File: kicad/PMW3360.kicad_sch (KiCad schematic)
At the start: 8 parts, among them J1 Conn_01x06, U1 PMW3360, U2 TCR2EF19

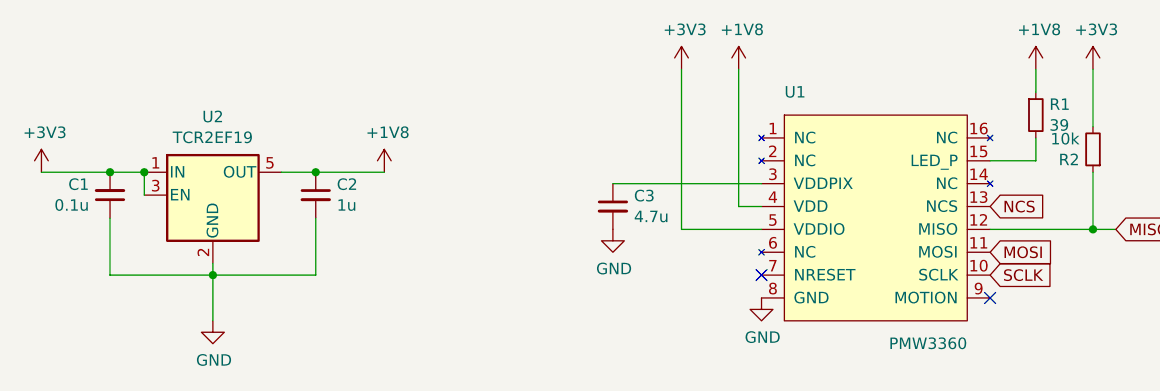
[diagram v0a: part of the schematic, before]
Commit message: Switched to JST_GH 1.25mm side-entry plug. Updated part info for the 1.8v regulator to the one that's actually available through JLCPCB.
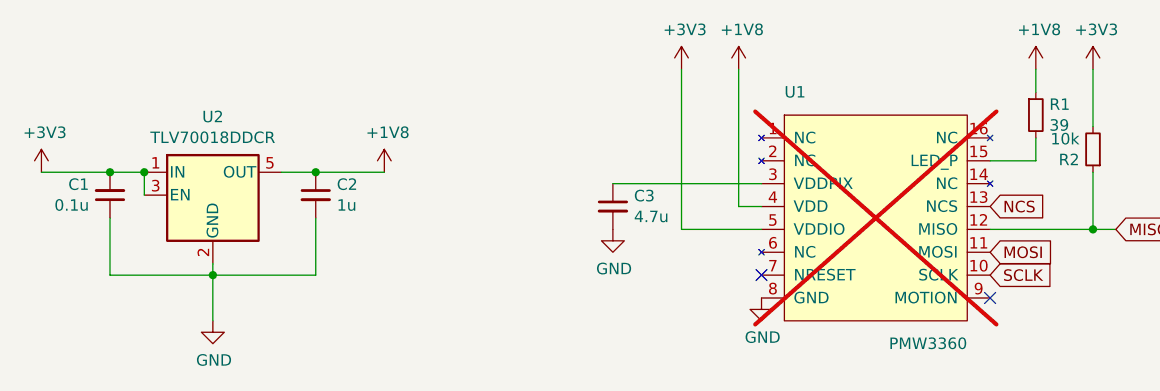
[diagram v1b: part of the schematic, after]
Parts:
- J1: footprint Connector_JST:JST_SH_BM06B-SRSS-TB_1x06-1MP_P1.00mm_Vertical -> Connector_JST:JST_GH_SM06B-GHS-TB_1x06-1MP_P1.25mm_Horizontal; LCSC (none) -> C133065
- U1: now not fitted
- U2: value TCR2EF19 -> TLV70018DDCR; symbol Regulator_Linear:TLV70218_SOT23-5 -> Regulator_Linear:TLV70018_SOT23-5; LCSC C146366 -> C79924
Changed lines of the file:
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@@
 		(in_bom yes)
 		(on_board yes)
-		(dnp no)
+		(dnp yes)
 		(property "Reference" "U1"
 			(at 133.35 86.36 0)
@@
 	)
 	(symbol
-		(lib_id "Regulator_Linear:TLV70218_SOT23-5")
+		(lib_id "Regulator_Linear:TLV70018_SOT23-5")
 		(at 69.85 97.79 0)
 		(unit 1)
@@
 			)
 		)
-		(property "Value" "TCR2EF19"
+		(property "Value" "TLV70018DDCR"
 			(at 69.85 91.4146 0)
 			(effects
@@
 			)
 		)
-		(property "Datasheet" ""
+		(property "Datasheet" "http://www.ti.com/lit/ds/symlink/tlv700.pdf"
 			(at 69.85 96.52 0)
 			(effects
@@
 			)
 		)
-		(property "Description" ""
+		(property "Description" "200mA Low Dropout Voltage Regulator, Fixed Output 1.8V, SOT-23-5"
 			(at 69.85 97.79 0)
 			(effects
@@
 			)
 		)
-		(property "LCSC" "C146366"
+		(property "LCSC" "C79924"
 			(at 69.85 97.79 0)
 			(effects
@@
 			)
 		)
-		(property "Footprint" "Connector_JST:JST_SH_BM06B-SRSS-TB_1x06-1MP_P1.00mm_Vertical"
+		(property "Footprint" "Connector_JST:JST_GH_SM06B-GHS-TB_1x06-1MP_P1.25mm_Horizontal"
 			(at 215.9 99.06 0)
 			(effects
@@
 			(at 215.9 99.06 0)
 			(effects
+				(font
+					(size 1.27 1.27)
+				)
+				(hide yes)
+			)
+		)
+		(property "LCSC" "C133065"
+			(at 215.9 99.06 0)
+			(effects

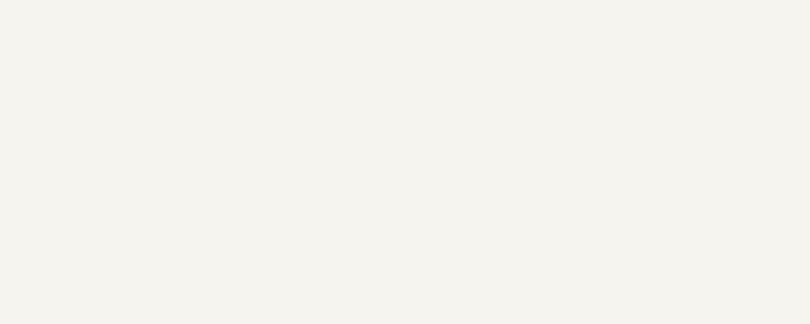
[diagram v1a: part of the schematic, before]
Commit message: Change back to JST SH 1.0mm pitch connector Use top-side 3.3v fill zone for simpler routing add .gitignore file
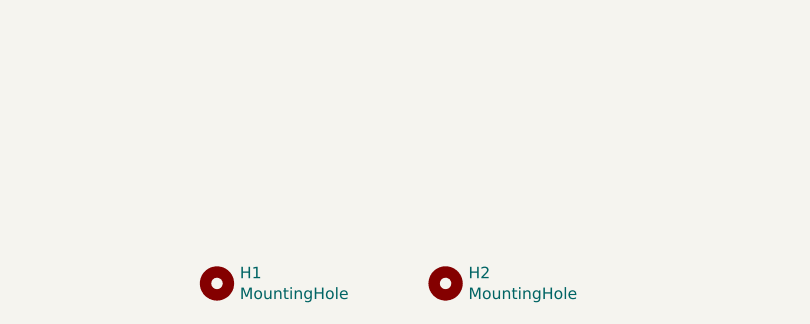
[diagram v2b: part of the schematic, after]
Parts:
- added H1, H2: MountingHole, MountingHole:MountingHole_2.2mm_M2, symbol Mechanical:MountingHole
- J1: footprint Connector_JST:JST_GH_SM06B-GHS-TB_1x06-1MP_P1.25mm_Horizontal -> Connector_JST:JST_SH_BM06B-SRSS-TB_1x06-1MP_P1.00mm_Vertical; LCSC C133065 -> C160392
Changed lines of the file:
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@@
 			)
 		)
-		(property "Footprint" "Connector_JST:JST_GH_SM06B-GHS-TB_1x06-1MP_P1.25mm_Horizontal"
+		(property "Footprint" "Connector_JST:JST_SH_BM06B-SRSS-TB_1x06-1MP_P1.00mm_Vertical"
 			(at 215.9 99.06 0)
 			(effects
@@
 			)
 		)
-		(property "Datasheet" "~"
+		(property "Datasheet" "https://www.lcsc.com/datasheet/lcsc_datasheet_2304140030_JST-BM06B-SRSS-TB-LF-SN_C160392.pdf"
 			(at 215.9 99.06 0)
 			(effects
@@
 			)
 		)
-		(property "LCSC" "C133065"
+		(property "LCSC" "C160392"
 			(at 215.9 99.06 0)
 			(effects
@@
 					(unit 1)
 				)
+			)
+		)
+	)
+	(symbol
+		(lib_id "Mechanical:MountingHole")
+		(at 80.01 187.96 0)
+		(unit 1)
+		(exclude_from_sim no)
+		(in_bom no)
+		(on_board yes)
+		(dnp no)
+		(property "Reference" "H1"
+			(at 82.55 186.7916 0)
+			(effects
+				(font
+					(size 1.27 1.27)
+				)
+				(justify left)
+			)
+		)
+		(property "Value" "MountingHole"
+			(at 82.55 189.103 0)
+			(effects
+				(font
+					(size 1.27 1.27)
+				)
+				(justify left)
+			)
+		)
+		(property "Footprint" "MountingHole:MountingHole_2.2mm_M2"
+			(at 80.01 187.96 0)
+			(effects
+				(font
+					(size 1.27 1.27)
+				)
+				(hide yes)
+			)
+		)
+		(property "Datasheet" "~"
+			(at 80.01 187.96 0)
+			(effects
+				(font
+					(size 1.27 1.27)
+				)
+				(hide yes)
+			)
+		)
+		(property "Description" ""
+			(at 80.01 187.96 0)
+			(effects
+				(font
+					(size 1.27 1.27)
+				)
+				(hide yes)
+			)
+		)
+		(instances
+			(project "PMW3360"
+				(path "/b3b0fc27-2485-4e75-b804-36148f2a5844"
+					(reference "H1")
+					(unit 1)
+				)
+			)
+		)
+	)
+	(symbol
+		(lib_id "Mechanical:MountingHole")
+		(at 105.41 187.96 0)
+		(unit 1)
+		(exclude_from_sim no)
+		(in_bom no)
+		(on_board yes)
+		(dnp no)
+		(property "Reference" "H2"
+			(at 107.95 186.7916 0)
+			(effects
+				(font
+					(size 1.27 1.27)
+				)
+				(justify left)
+			)
+		)
+		(property "Value" "MountingHole"
+			(at 107.95 189.103 0)
+			(effects
+				(font
+					(size 1.27 1.27)
+				)
+				(justify left)
+			)
+		)
+		(property "Footprint" "MountingHole:MountingHole_2.2mm_M2"
+			(at 105.41 187.96 0)
+			(effects
+				(font
+					(size 1.27 1.27)
+				)
+				(hide yes)
+			)
+		)
+		(property "Datasheet" "~"
+			(at 105.41 187.96 0)
+			(effects
+				(font
+					(size 1.27 1.27)
+				)
+				(hide yes)
+			)
+		)
+		(property "Description" ""
+			(at 105.41 187.96 0)
+			(effects
+				(font
+					(size 1.27 1.27)
+				)
+				(hide yes)
+			)
+		)
+		(property "LCSC" ""
+			(at 105.41 187.96 0)
+			(effects
+				(font
+					(size 1.27 1.27)
+				)
+				(hide yes)
+			)
+		)
+		(instances
+			(project "PMW3360"
+				(path "/b3b0fc27-2485-4e75-b804-36148f2a5844"
+					(reference "H2")
+					(unit 1)
+				)

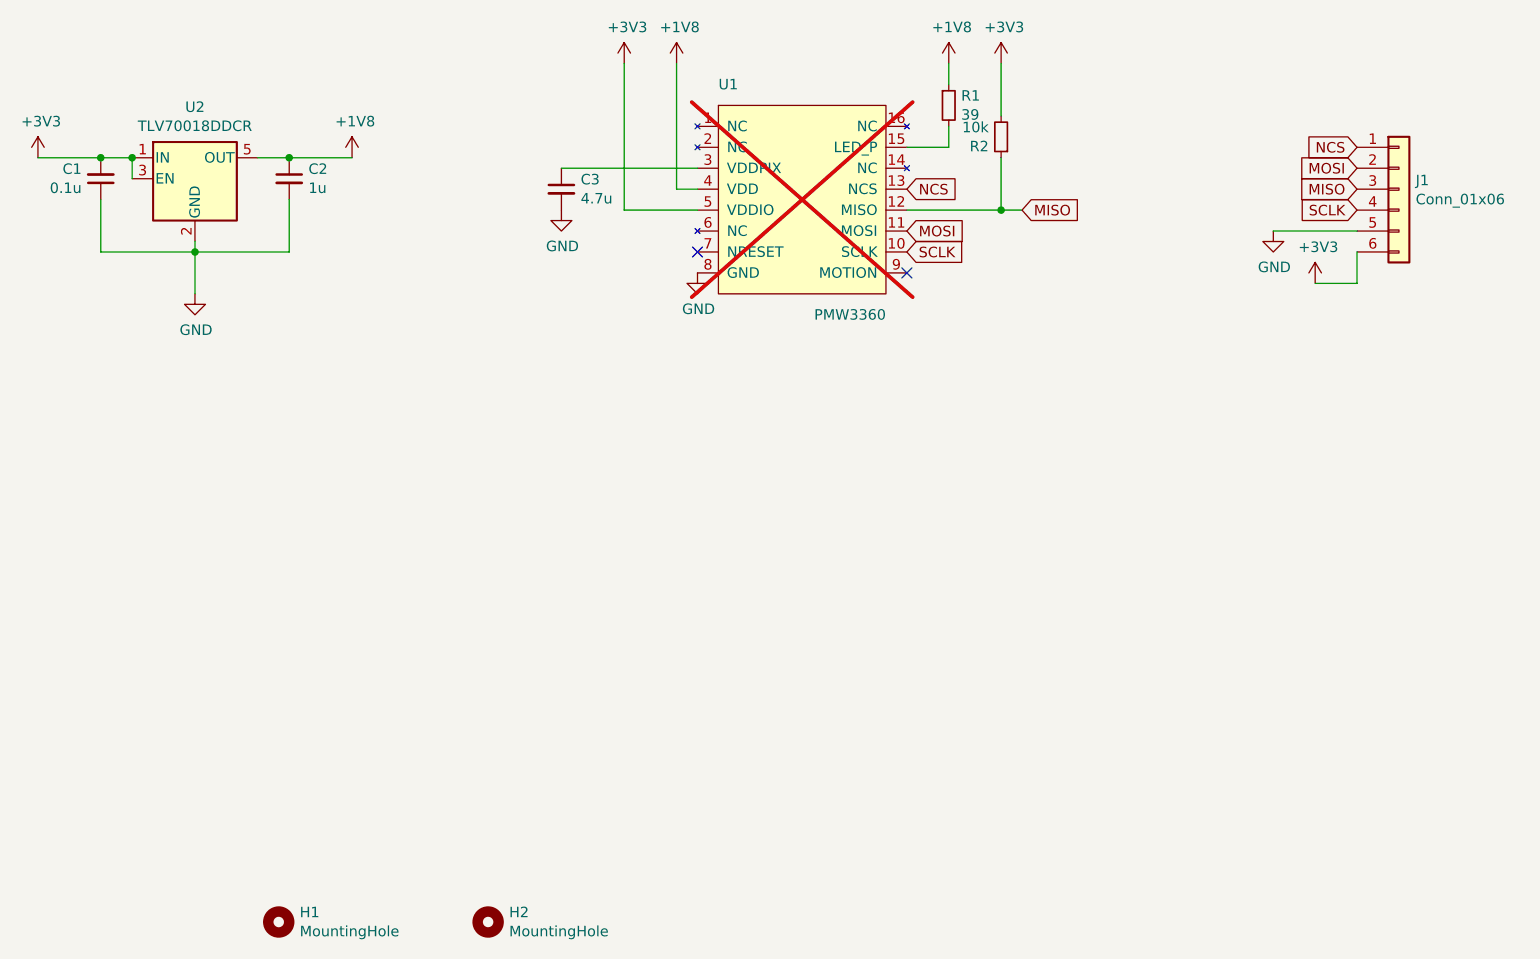
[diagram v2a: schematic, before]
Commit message: Make more symmetrical. Clean up silkscreens a bit. Add a pad for the motion line.
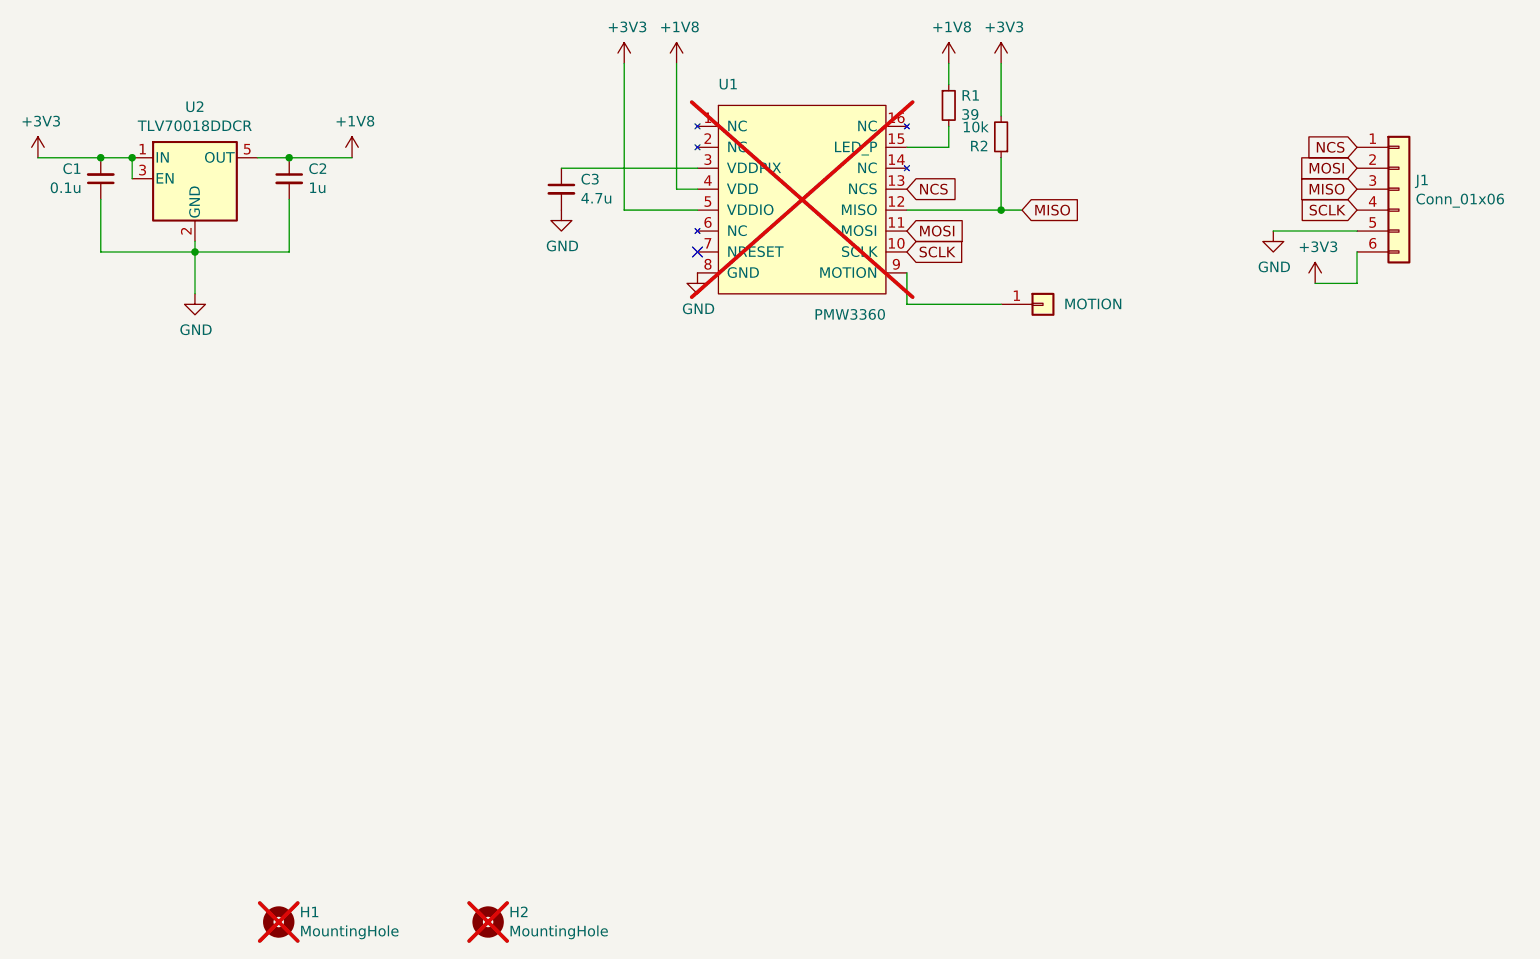
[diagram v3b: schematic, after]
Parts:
- added J2: MOTION, Connector_PinSocket_2.54mm:PinSocket_1x01_P2.54mm_Vertical, symbol Connector_Generic:Conn_01x01
- H1, H2: now not fitted
- J1: footprint Connector_JST:JST_SH_BM06B-SRSS-TB_1x06-1MP_P1.00mm_Vertical -> PMW3360:JST_SH_BM06B-SRSS-TB_1x06-1MP_P1.00mm_Vertical; LCSC C160392 -> C7430455
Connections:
- net at U1.9 (MOTION): now also J2.1 (Pin_1)
- no-connect marks 2 -> 1
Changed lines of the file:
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@@
-	)
-	(no_connect
-		(at 156.21 109.22)
 	)
 	(no_connect
@@
 	(wire
 		(pts
+			(xy 167.64 113.03) (xy 156.21 113.03)
+		)
+		(stroke
+			(width 0)
+			(type default)
+		)
+	)
+	(wire
+		(pts
 			(xy 130.81 101.6) (xy 121.92 101.6)
 		)
@@
 		(pts
 			(xy 205.74 110.49) (xy 210.82 110.49)
+		)
+		(stroke
+			(width 0)
+			(type default)
+		)
+	)
+	(wire
+		(pts
+			(xy 156.21 113.03) (xy 156.21 109.22)
 		)
 		(stroke
@@
 			)
 		)
-		(property "Footprint" "Connector_JST:JST_SH_BM06B-SRSS-TB_1x06-1MP_P1.00mm_Vertical"
+		(property "Footprint" "PMW3360:JST_SH_BM06B-SRSS-TB_1x06-1MP_P1.00mm_Vertical"
 			(at 215.9 99.06 0)
 			(effects
@@
 			)
 		)
-		(property "LCSC" "C160392"
+		(property "LCSC" "C7430455"
 			(at 215.9 99.06 0)
 			(effects
@@
 		(in_bom no)
 		(on_board yes)
-		(dnp no)
+		(dnp yes)
 		(property "Reference" "H1"
 			(at 82.55 186.7916 0)
@@
 	)
 	(symbol
+		(lib_id "Connector_Generic:Conn_01x01")
+		(at 172.72 113.03 0)
+		(unit 1)
+		(exclude_from_sim no)
+		(in_bom yes)
+		(on_board yes)
+		(dnp no)
+		(fields_autoplaced yes)
+		(property "Reference" "J2"
+			(at 175.26 111.7599 0)
+			(effects
+				(font
+					(size 1.27 1.27)
+				)
+				(justify left)
+				(hide yes)
+			)
+		)
+		(property "Value" "MOTION"
+			(at 175.26 113.0299 0)
+			(effects
+				(font
+					(size 1.27 1.27)
+				)
+				(justify left)
+			)
+		)
+		(property "Footprint" "Connector_PinSocket_2.54mm:PinSocket_1x01_P2.54mm_Vertical"
+			(at 172.72 113.03 0)
+			(effects
+				(font
+					(size 1.27 1.27)
+				)
+				(hide yes)
+			)
+		)
+		(property "Datasheet" "~"
+			(at 172.72 113.03 0)
+			(effects
+				(font
+					(size 1.27 1.27)
+				)
+				(hide yes)
+			)
+		)
+		(property "Description" "Generic connector, single row, 01x01, script generated (kicad-library-utils/schlib/autogen/connector/)"
+			(at 172.72 113.03 0)
+			(effects
+				(font
+					(size 1.27 1.27)
+				)
+				(hide yes)
+			)
+		)
+		(property "LCSC" ""
+			(at 172.72 113.03 0)
+			(effects
+				(font
+					(size 1.27 1.27)
+				)
+				(hide yes)
+			)
+		)
+		(pin "1"
+		)
+		(instances
+			(project ""
+				(path "/b3b0fc27-2485-4e75-b804-36148f2a5844"
+					(reference "J2")
+					(unit 1)
+				)
+			)
+		)
+	)
+	(symbol
 		(lib_id "Mechanical:MountingHole")
 		(at 105.41 187.96 0)
@@
 		(in_bom no)
 		(on_board yes)
-		(dnp no)
+		(dnp yes)
 		(property "Reference" "H2"
 			(at 107.95 186.7916 0)
